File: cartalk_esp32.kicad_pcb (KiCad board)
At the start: 2 copper layers, 21.3 x 48.8 mm, 22 parts, among them IC1 CP2104, J1 10118192-0002LF, Q1 mmbt2222, Q2 mmbt2222, SW2 KMR2, U1 HUB75 Connector Female, U2 AP2112-3.3, X2 ESP32_WROOM32_SKINNY

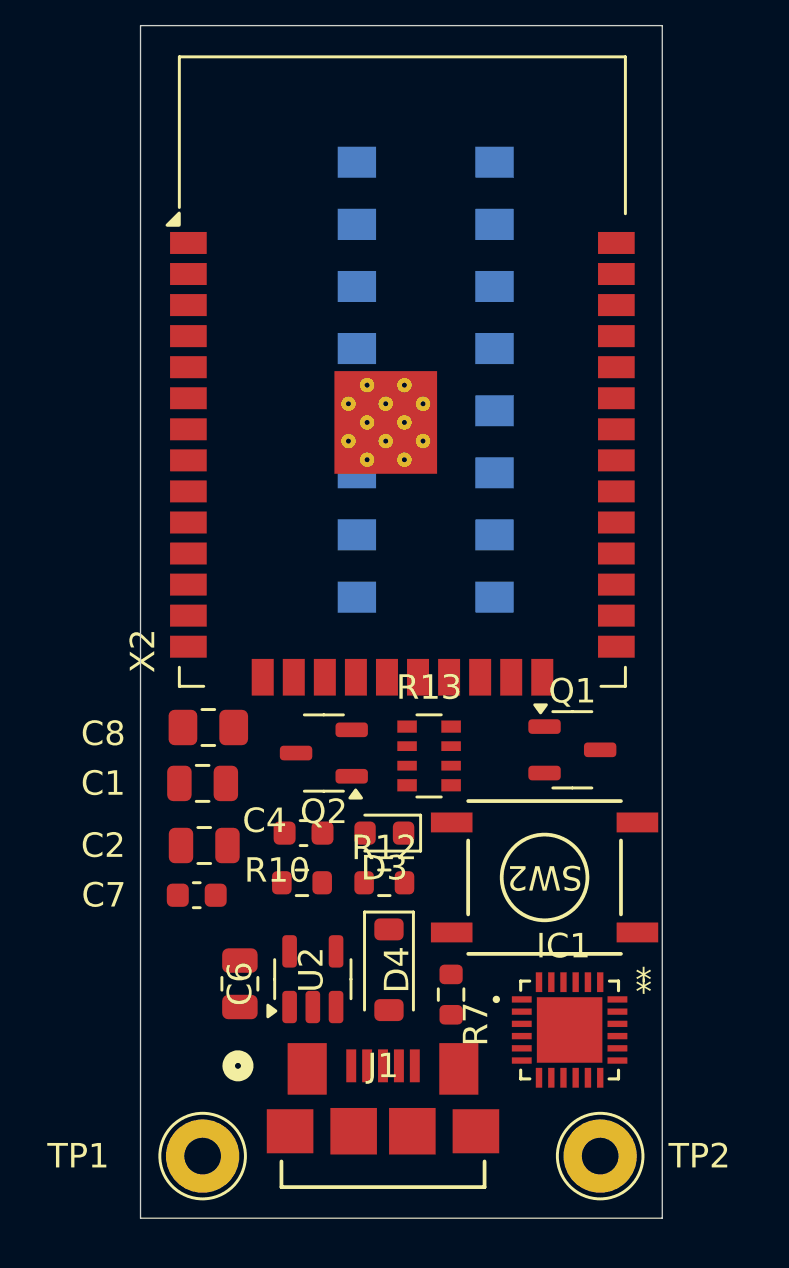
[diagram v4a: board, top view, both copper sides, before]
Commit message: Route tracks on the top layer.
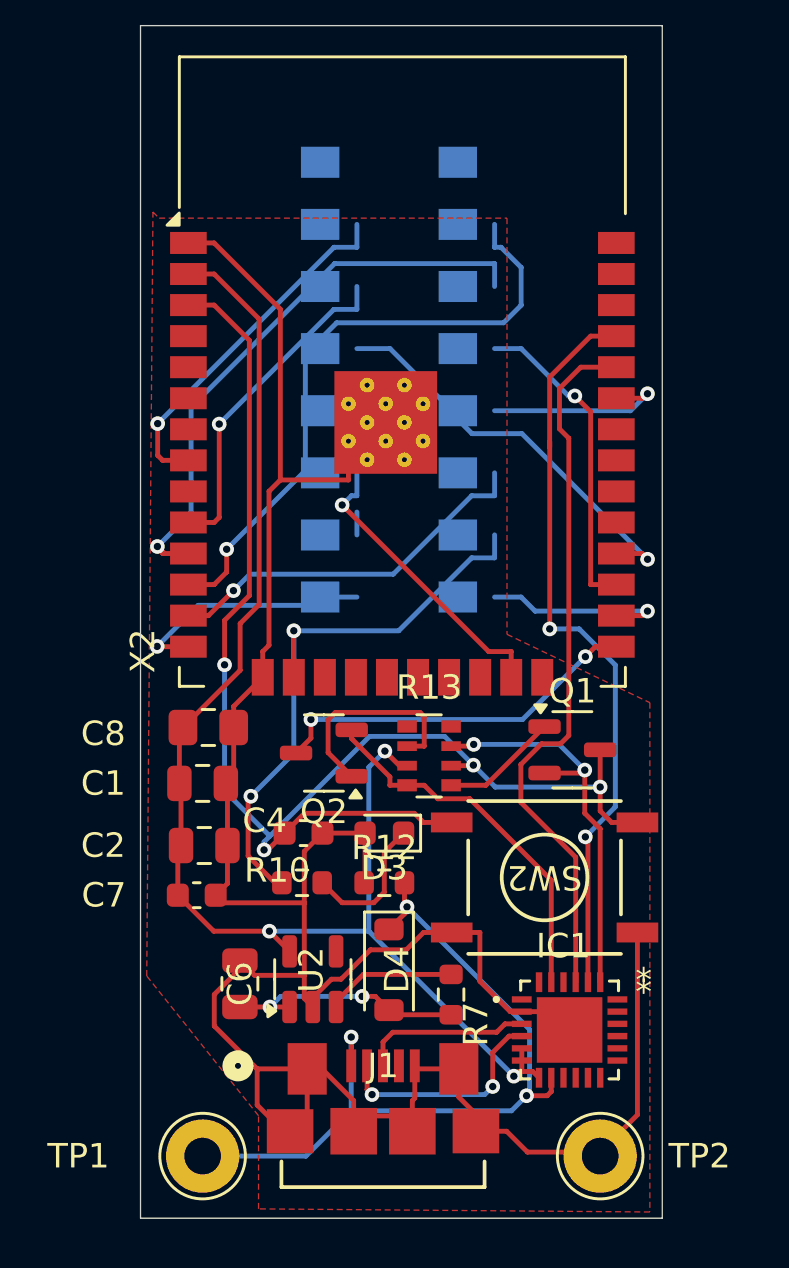
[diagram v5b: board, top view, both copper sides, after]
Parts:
- moved U1 1.50 mm to (129.0, 95.2)
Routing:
- net GND: track 0.00 -> 128.2 mm
- net 3.3V: track 0.00 -> 57.6 mm, vias 0 -> 3
- net /RESET: track 0.00 -> 54.9 mm, vias 0 -> 4
- net VBUS: track 0.00 -> 32.2 mm, vias 0 -> 3
- net /TXD0: track 0.00 -> 30.8 mm, vias 0 -> 2
- net /RXD0: track 0.00 -> 29.3 mm
- net /LED_CLK: track 0.00 -> 25.6 mm, vias 0 -> 1
- net /B1: track 0.00 -> 24.1 mm, vias 0 -> 2
- net /ADDR_C: track 0.00 -> 23.5 mm, vias 0 -> 1
- net /ADDR_B: track 0.00 -> 16.9 mm, vias 0 -> 1
- net /RTS: track 0.00 -> 16.5 mm, vias 0 -> 2
- net /R2: track 0.00 -> 15.5 mm, vias 0 -> 1
- net /GPIO0: track 0.00 -> 15.3 mm, vias 0 -> 2
- net /DTR: track 0.00 -> 15.3 mm
- net /STROBE: track 0.00 -> 14.7 mm, vias 0 -> 1
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- added copper zone on F.Cu, net GND

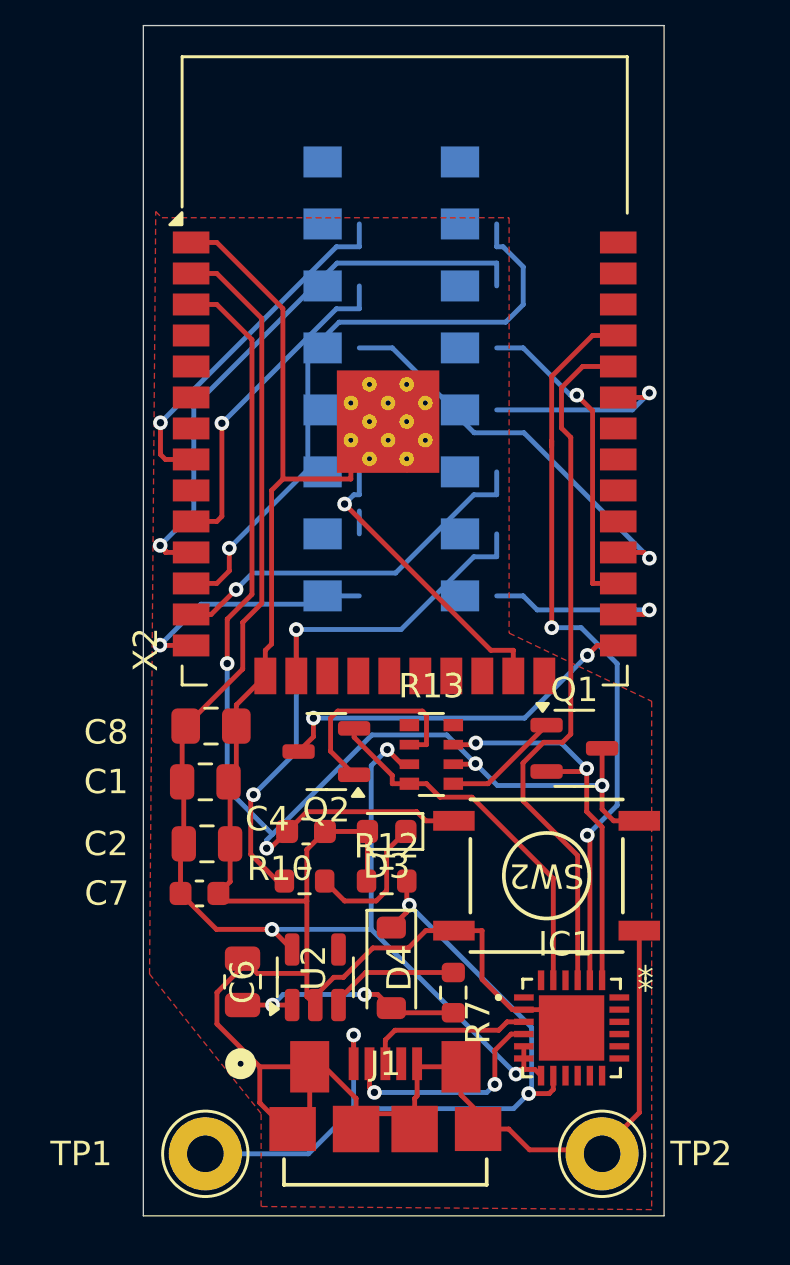
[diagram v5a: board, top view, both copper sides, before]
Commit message: Route tracks that autorouter couldn't figure out.
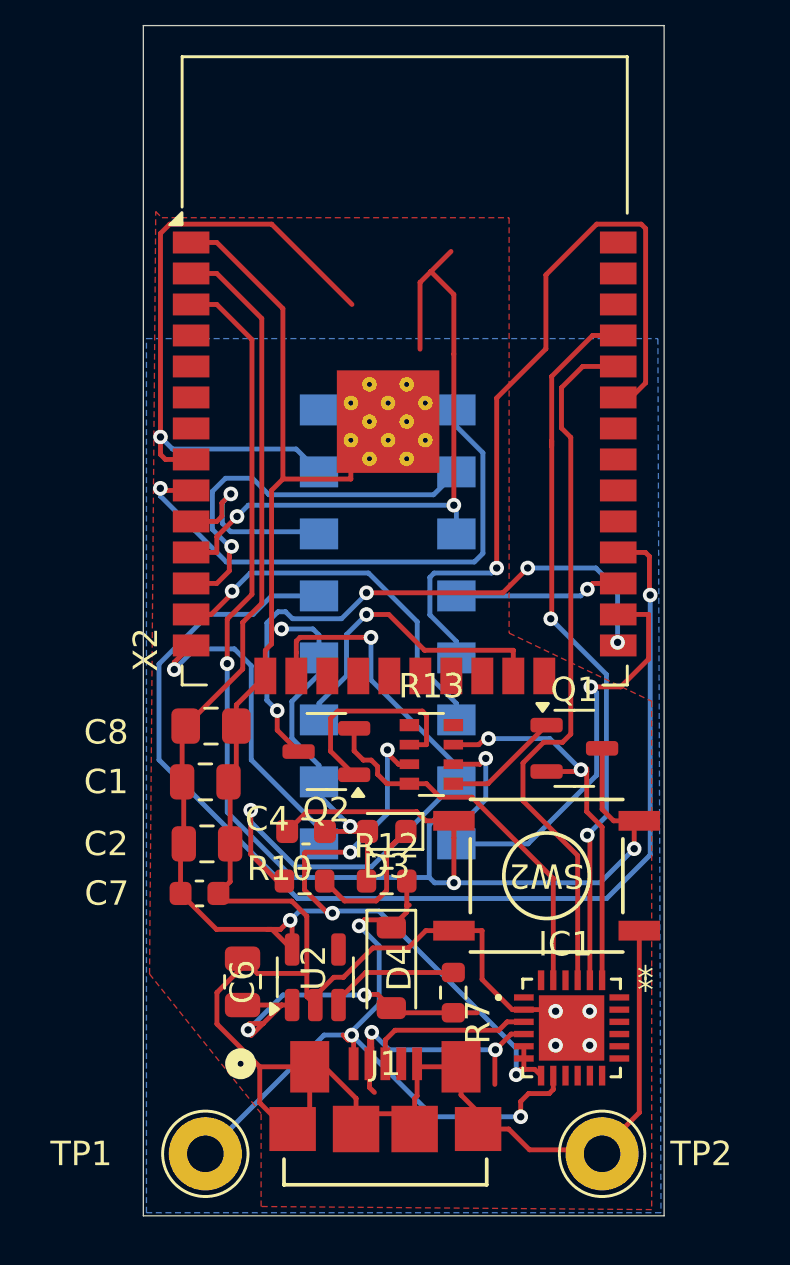
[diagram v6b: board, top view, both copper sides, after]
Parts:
- moved U1 10.2 mm to (128.9, 105.4)
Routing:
- net /ADDR_B: track 16.9 -> 48.4 mm
- net /B2: track 7.89 -> 32.2 mm
- net /LED_~{OE}: track 0.00 -> 22.7 mm, vias 0 -> 1
- net /STROBE: track 14.7 -> 26.9 mm
- net /RESET: track 54.9 -> 65.0 mm
- net /LED_CLK: track 25.6 -> 16.3 mm
- net /GPIO0: track 15.3 -> 24.4 mm, vias 2 -> 4
- net /R1: track 7.84 -> 16.5 mm
- net /ADDR_A: track 13.1 -> 6.86 mm
- net /ADDR_D: track 13.7 -> 7.91 mm
- net 3.3V: track 57.6 -> 62.7 mm, vias 3 -> 5
- net Net-(D4-C): track 9.93 -> 15.0 mm
- net /ADDR_C: track 23.5 -> 27.7 mm, vias 1 -> 2
- net /G1: track 10.3 -> 13.5 mm
- net /B1: track 24.1 -> 26.7 mm
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- added copper zone on B.Cu, net GND

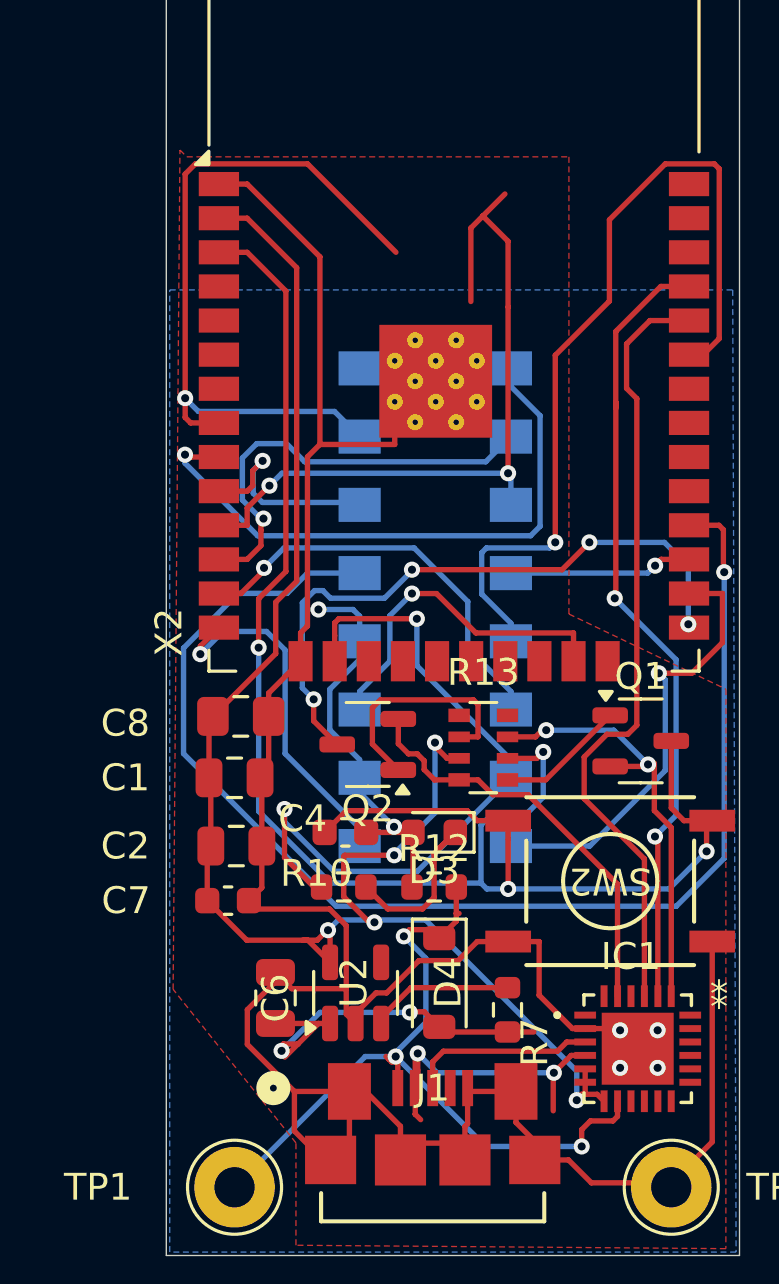
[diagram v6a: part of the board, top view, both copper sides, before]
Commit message: Clean up remaining track fingers.
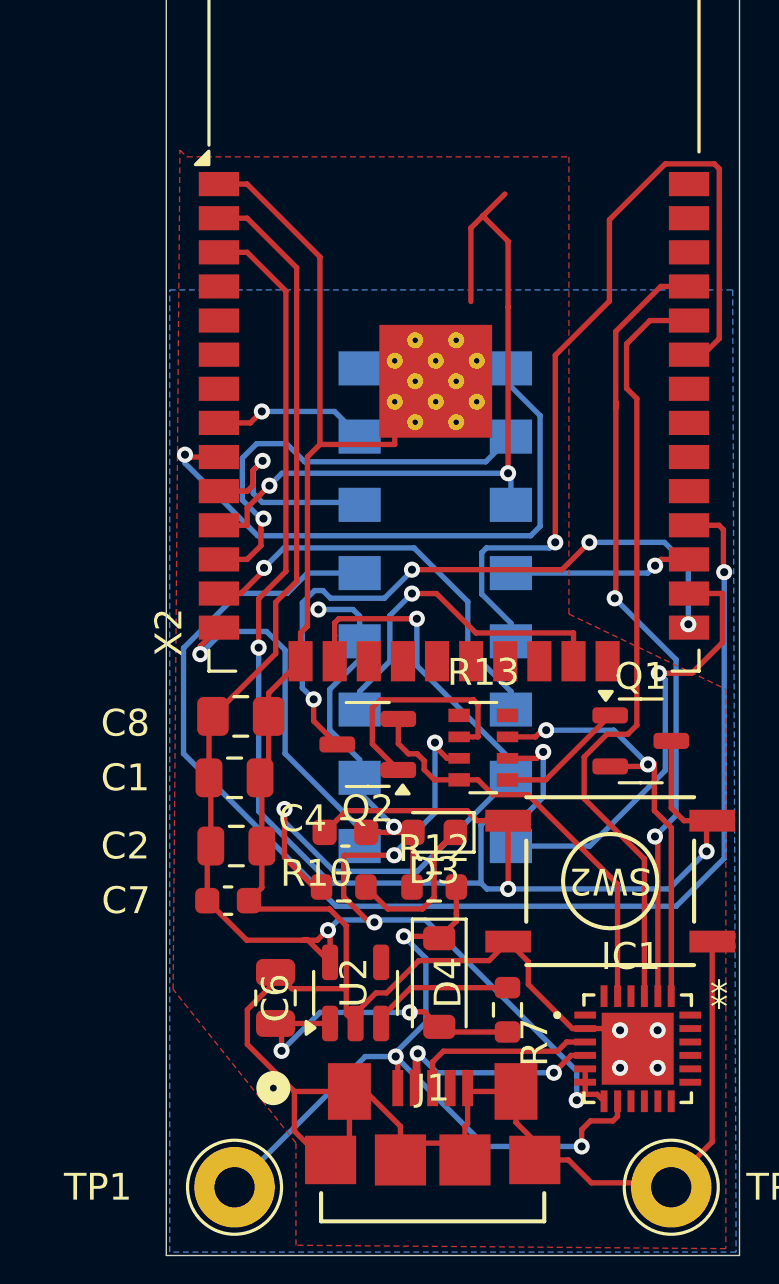
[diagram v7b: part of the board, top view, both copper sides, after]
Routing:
- net /STROBE: track 26.9 -> 5.80 mm
- net Net-(IC1A-D-): track 11.4 -> 8.75 mm
- net Net-(D4-C): track 15.0 -> 12.5 mm
- net VBUS: track 30.7 -> 29.6 mm
- net GND: track 128.2 -> 127.5 mm
